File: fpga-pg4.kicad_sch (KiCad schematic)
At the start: 23 parts, among them U6 XC7A15T-CSG325

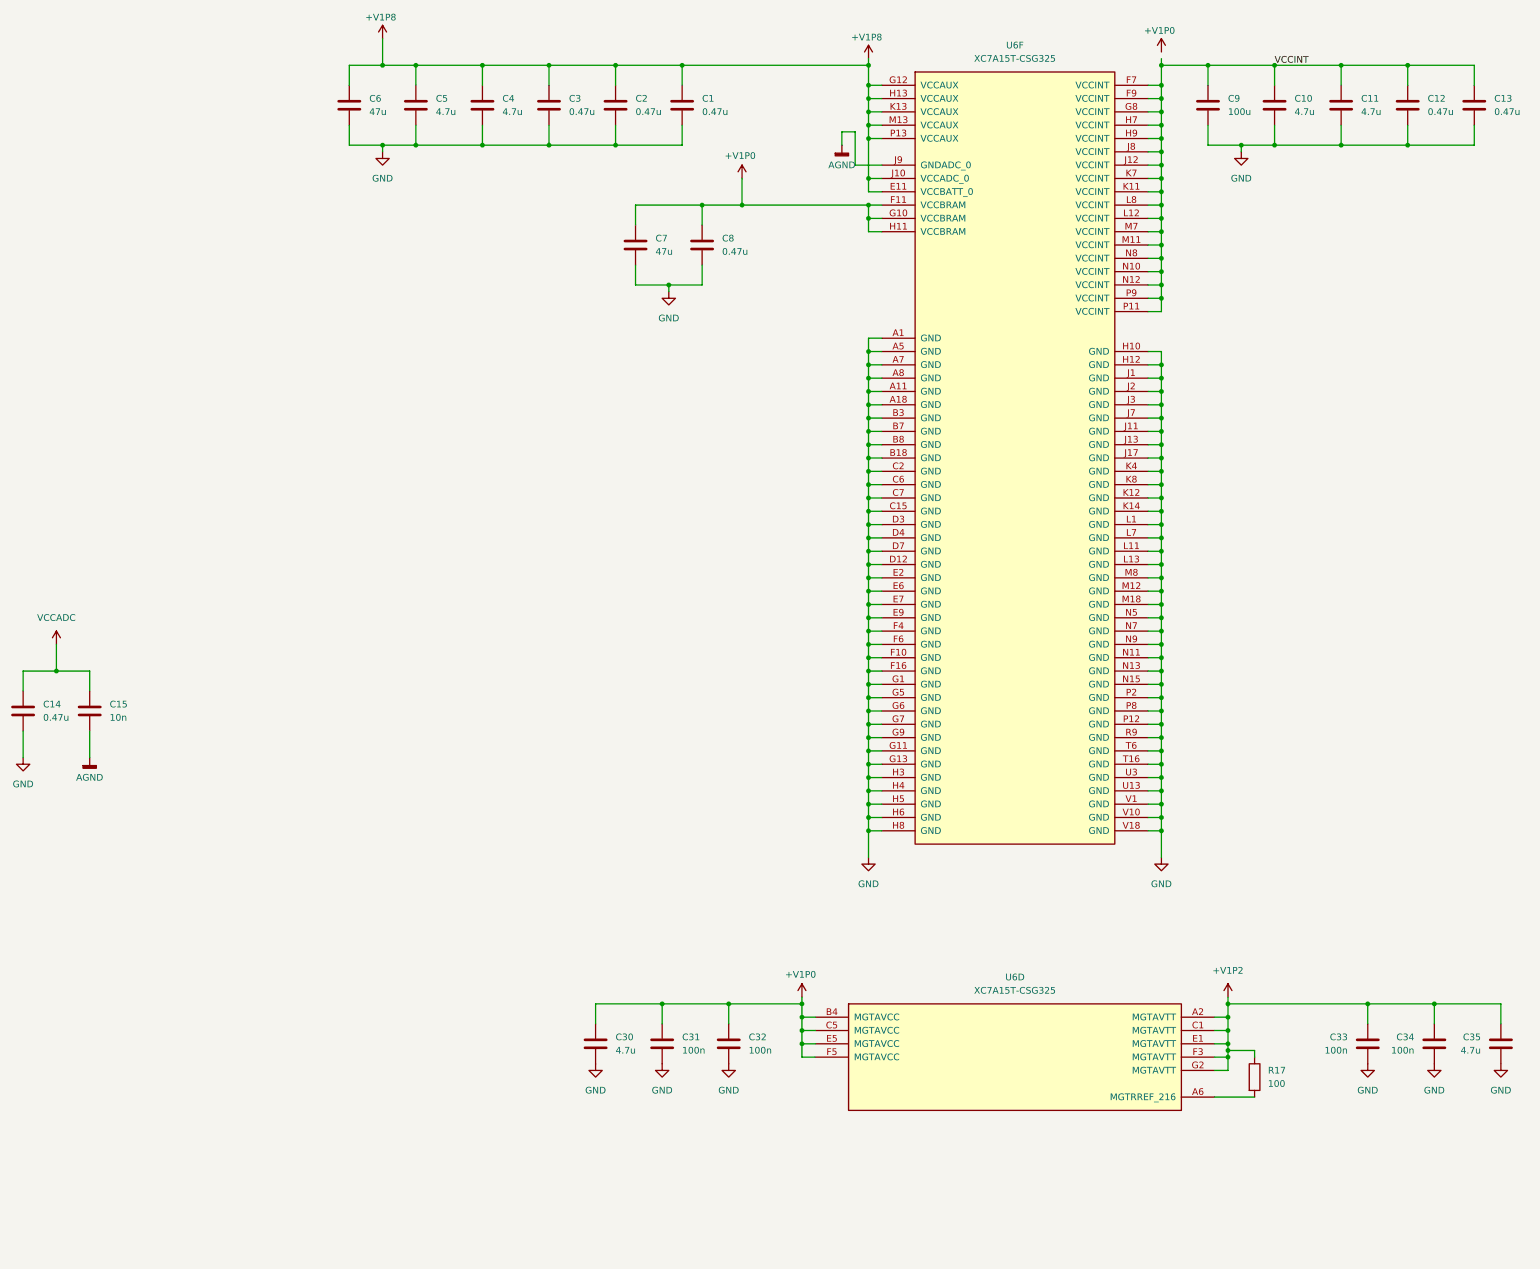
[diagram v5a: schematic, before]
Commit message: started changing package, added correct decoupling
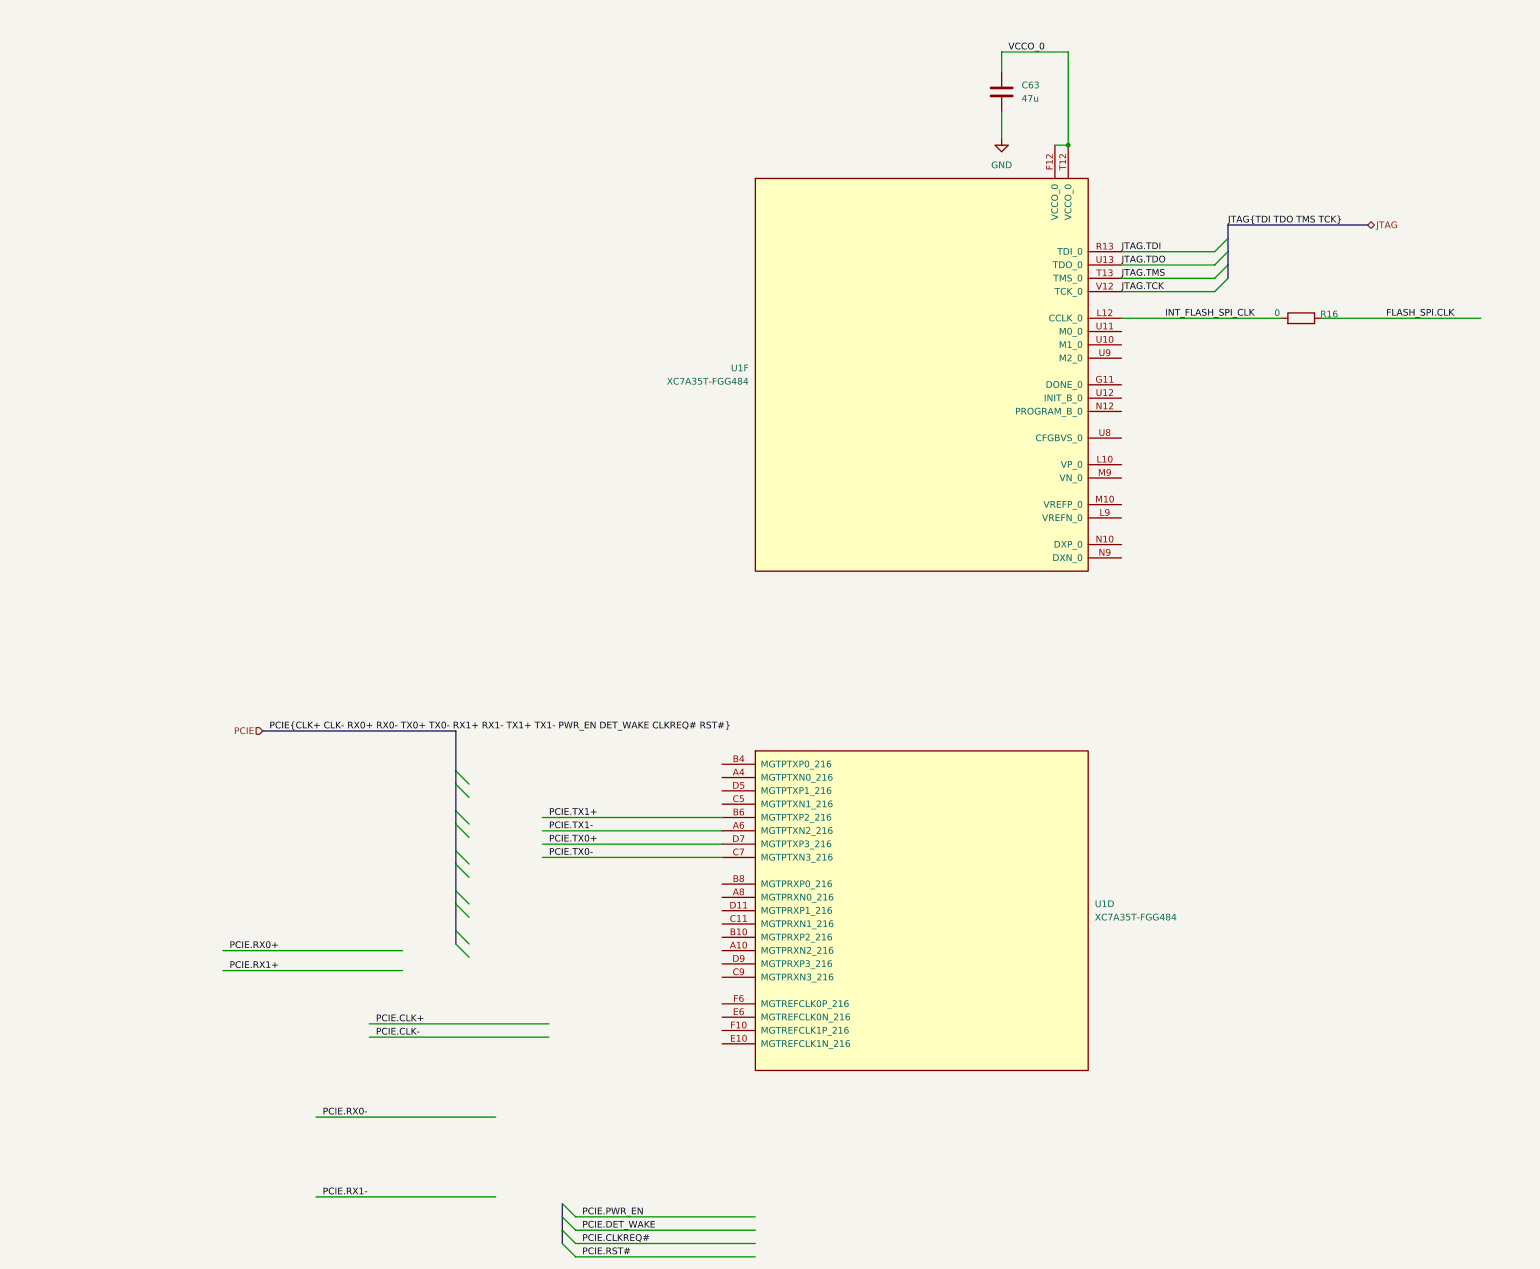
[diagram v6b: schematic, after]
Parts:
- removed C1, C12, C13, C14, C2, C3, C8: 0.47u, Capacitor_SMD:C_0402_1005Metric, symbol Device:C
- removed C10, C11, C30, C35, C4, C5: 4.7u, Capacitor_SMD:C_0402_1005Metric, symbol Device:C
- removed C15: 10n, Capacitor_SMD:C_0402_1005Metric, symbol Device:C
- removed C31, C32, C33, C34: 100n, Capacitor_SMD:C_0402_1005Metric, symbol Device:C
- removed C6, C7: 47u, Capacitor_SMD:C_1210_3225Metric, symbol Device:C
- removed C9: 100u, Capacitor_SMD:C_1210_3225Metric, symbol Device:C
- removed R17: 100, Capacitor_SMD:C_0402_1005Metric, symbol Device:R
- removed U6: XC7A15T-CSG325, Package_BGA:Xilinx_CSG325, symbol FPGA_Xilinx_Artix7:XC7A15T-CSG325
- added C63: 47u, Capacitor_SMD:C_1210_3225Metric, symbol Device:C
- added R16: 0, Resistor_SMD:R_0402_1005Metric_Pad0.72x0.64mm_HandSolder, symbol Device:R
- added U1: XC7A35T-FGG484, Package_BGA:Xilinx_FGG484, symbol FPGA_Xilinx_Artix7:XC7A35T-FGG484
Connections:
- net GND: now also C63.2
- new net FLASH_SPI.CLK: R16.1
- new net INT_FLASH_SPI_CLK: R16.2, U1.L12 (CCLK_0)
- new net JTAG.TCK: U1.V12 (TCK_0)
- new net JTAG.TDI: U1.R13 (TDI_0)
- new net JTAG.TDO: U1.U13 (TDO_0)
- new net JTAG.TMS: U1.T13 (TMS_0)
- new net PCIE.TX0+: U1.D7 (MGTPTXP3_216)
- new net PCIE.TX0-: U1.C7 (MGTPTXN3_216)
- new net PCIE.TX1+: U1.B6 (MGTPTXP2_216)
- new net PCIE.TX1-: U1.A6 (MGTPTXN2_216)
- new net VCCO_0: C63.1, U1.F12 (VCCO_0), U1.T12 (VCCO_0)

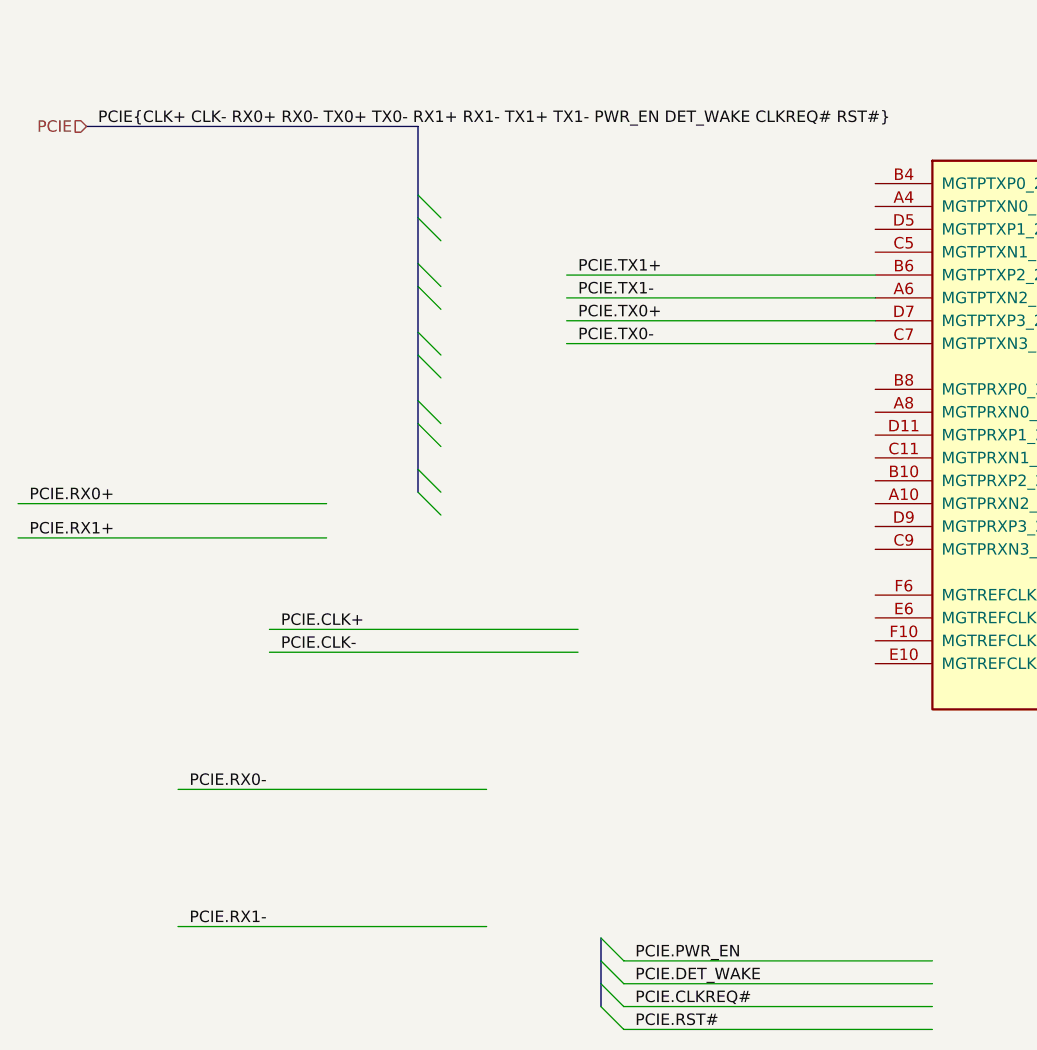
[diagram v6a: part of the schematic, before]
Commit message: filled out back connector, finished ddr pinning according to vivado
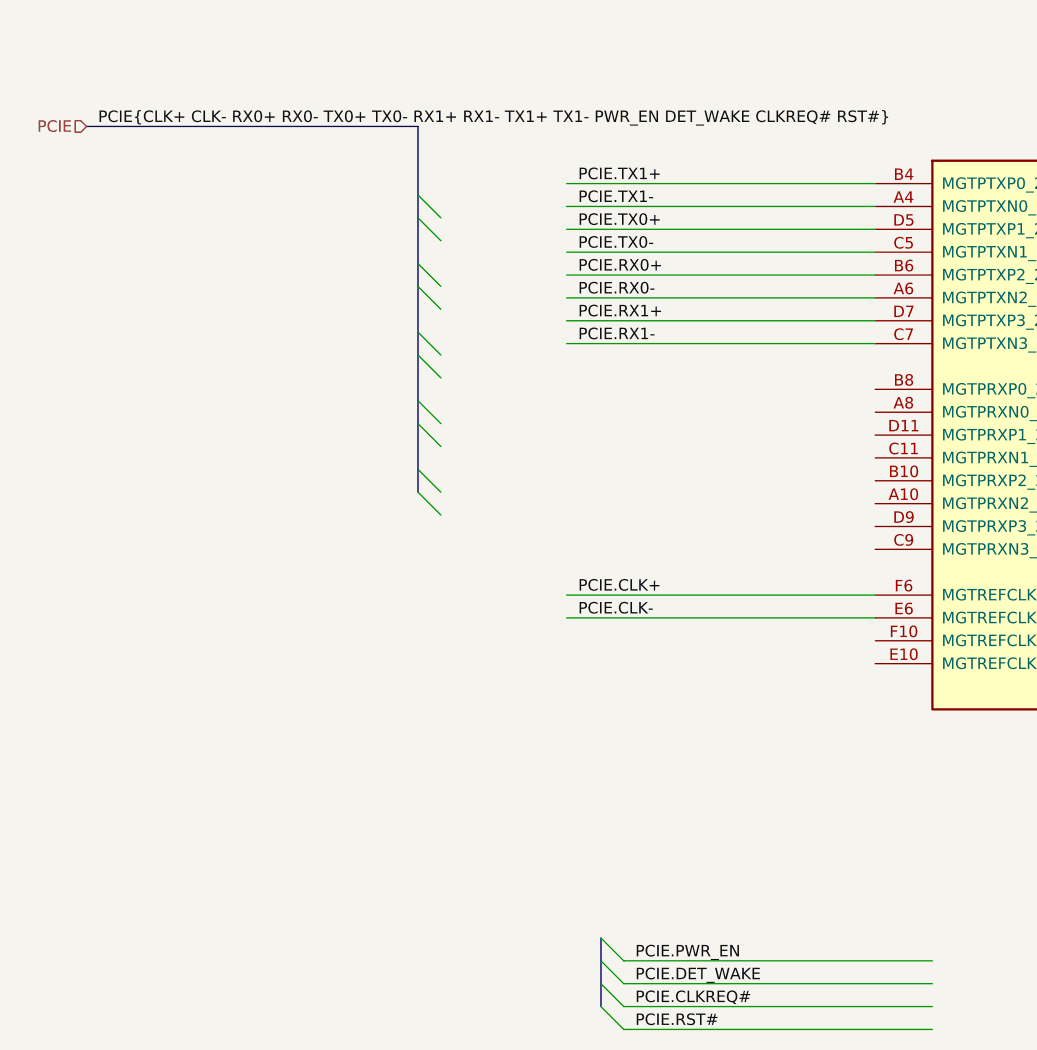
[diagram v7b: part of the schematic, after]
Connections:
- net PCIE.CLK+: now also U1.F6 (MGTREFCLK0P_216)
- net PCIE.CLK-: now also U1.E6 (MGTREFCLK0N_216)
- net PCIE.RX0+: now also U1.B6 (MGTPTXP2_216)
- net PCIE.RX0-: now also U1.A6 (MGTPTXN2_216)
- net PCIE.RX1+: now also U1.D7 (MGTPTXP3_216)
- net PCIE.RX1-: now also U1.C7 (MGTPTXN3_216)
- net PCIE.TX0+: now also U1.D5 (MGTPTXP1_216); no longer U1.D7 (MGTPTXP3_216)
- net PCIE.TX0-: now also U1.C5 (MGTPTXN1_216); no longer U1.C7 (MGTPTXN3_216)
- net PCIE.TX1+: now also U1.B4 (MGTPTXP0_216); no longer U1.B6 (MGTPTXP2_216)
- net PCIE.TX1-: now also U1.A4 (MGTPTXN0_216); no longer U1.A6 (MGTPTXN2_216)
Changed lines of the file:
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@@
+	(wire
+		(pts
+			(xy 137.16 168.91) (xy 171.45 168.91)
+		)
+		(stroke
+			(width 0)
+			(type default)
+		)
+	)
 	(wire
 		(pts
@@
 		)
 	)
+	(wire
+		(pts
+			(xy 137.16 176.53) (xy 171.45 176.53)
+		)
+		(stroke
+			(width 0)
+			(type default)
+		)
+	)
 	(bus
 		(pts
@@
 	(wire
 		(pts
+			(xy 247.65 71.12) (xy 265.43 71.12)
+		)
+		(stroke
+			(width 0)
+			(type default)
+		)
+	)
+	(bus
+		(pts
+			(xy 267.97 71.12) (xy 267.97 68.58)
+		)
+		(stroke
+			(width 0)
+			(type default)
+		)
+	)
+	(bus
+		(pts
+			(xy 140.97 257.81) (xy 140.97 260.35)
+		)
+		(stroke
+			(width 0)
+			(type default)
+		)
+	)
+	(wire
+		(pts
+			(xy 143.51 255.27) (xy 177.8 255.27)
+		)
+		(stroke
+			(width 0)
+			(type default)
+		)
+	)
+	(wire
+		(pts
+			(xy 247.65 78.74) (xy 265.43 78.74)
+		)
+		(stroke
+			(width 0)
+			(type default)
+		)
+	)
+	(wire
+		(pts
+			(xy 247.65 73.66) (xy 265.43 73.66)
+		)
+		(stroke
+			(width 0)
+			(type default)
+		)
+	)
+	(wire
+		(pts
 			(xy 137.16 179.07) (xy 171.45 179.07)
 		)
@@
 		)
 	)
-	(wire
-		(pts
-			(xy 247.65 71.12) (xy 265.43 71.12)
-		)
-		(stroke
-			(width 0)
-			(type default)
-		)
-	)
-	(bus
-		(pts
-			(xy 267.97 71.12) (xy 267.97 68.58)
-		)
-		(stroke
-			(width 0)
-			(type default)
-		)
-	)
-	(wire
-		(pts
-			(xy 76.2 204.47) (xy 110.49 204.47)
-		)
-		(stroke
-			(width 0)
-			(type default)
-		)
-	)
-	(bus
-		(pts
-			(xy 140.97 257.81) (xy 140.97 260.35)
-		)
-		(stroke
-			(width 0)
-			(type default)
-		)
-	)
-	(wire
-		(pts
-			(xy 143.51 255.27) (xy 177.8 255.27)
-		)
-		(stroke
-			(width 0)
-			(type default)
-		)
-	)
-	(wire
-		(pts
-			(xy 247.65 78.74) (xy 265.43 78.74)
-		)
-		(stroke
-			(width 0)
-			(type default)
-		)
-	)
-	(wire
-		(pts
-			(xy 247.65 73.66) (xy 265.43 73.66)
-		)
-		(stroke
-			(width 0)
-			(type default)
-		)
-	)
-	(wire
-		(pts
-			(xy 93.98 251.46) (xy 128.27 251.46)
-		)
-		(stroke
-			(width 0)
-			(type default)
-		)
-	)
 	(bus
 		(pts
@@
 	(wire
 		(pts
-			(xy 93.98 236.22) (xy 128.27 236.22)
+			(xy 137.16 171.45) (xy 171.45 171.45)
 		)
 		(stroke
@@
 		)
 	)
+	(wire
+		(pts
+			(xy 137.16 181.61) (xy 171.45 181.61)
+		)
+		(stroke
+			(width 0)
+			(type default)
+		)
+	)
 	(bus
 		(pts
@@
 		)
 	)
+	(bus
+		(pts
+			(xy 120.65 193.04) (xy 120.65 195.58)
+		)
+		(stroke
+			(width 0)
+			(type default)
+		)
+	)
+	(wire
+		(pts
+			(xy 278.13 83.82) (xy 247.65 83.82)
+		)
+		(stroke
+			(width 0)
+			(type default)
+		)
+	)
 	(wire
 		(pts
@@
 	(wire
 		(pts
-			(xy 137.16 181.61) (xy 171.45 181.61)
-		)
-		(stroke
-			(width 0)
-			(type default)
-		)
-	)
-	(bus
-		(pts
-			(xy 120.65 193.04) (xy 120.65 195.58)
-		)
-		(stroke
-			(width 0)
-			(type default)
-		)
-	)
-	(wire
-		(pts
-			(xy 278.13 83.82) (xy 247.65 83.82)
+			(xy 137.16 184.15) (xy 171.45 184.15)
 		)
 		(stroke
@@
 	(wire
 		(pts
-			(xy 104.14 218.44) (xy 138.43 218.44)
+			(xy 137.16 214.63) (xy 171.45 214.63)
 		)
 		(stroke
@@
 		)
 	)
+	(wire
+		(pts
+			(xy 137.16 173.99) (xy 171.45 173.99)
+		)
+		(stroke
+			(width 0)
+			(type default)
+		)
+	)
 	(bus
 		(pts
@@
 		)
 	)
-	(wire
-		(pts
-			(xy 137.16 184.15) (xy 171.45 184.15)
-		)
-		(stroke
-			(width 0)
-			(type default)
-		)
-	)
 	(bus
 		(pts
@@
 	(wire
 		(pts
-			(xy 104.14 220.98) (xy 138.43 220.98)
+			(xy 137.16 217.17) (xy 171.45 217.17)
 		)
 		(stroke
@@
 		)
 	)
-	(wire
-		(pts
-			(xy 76.2 208.28) (xy 110.49 208.28)
-		)
-		(stroke
-			(width 0)
-			(type default)
-		)
-	)
 	(bus
 		(pts
@@
 			(width 0)
 			(type default)
-		)
-	)
-	(label "PCIE.RX1+"
-		(at 77.47 208.28 0)
-		(effects
-			(font
-				(size 1.27 1.27)
-			)
-			(justify left bottom)
 		)
 	)
@@
 		)
 	)
+	(label "PCIE.CLK-"
+		(at 138.43 217.17 0)
+		(effects
+			(font
+				(size 1.27 1.27)
+			)
+			(justify left bottom)
+		)
+	)
+	(label "PCIE.TX0+"
+		(at 138.43 173.99 0)
+		(effects
+			(font
+				(size 1.27 1.27)
+			)
+			(justify left bottom)
+		)
+	)
 	(label "PCIE.TX0-"
-		(at 138.43 186.69 0)
-		(effects
-			(font
-				(size 1.27 1.27)
-			)
-			(justify left bottom)
-		)
-	)
-	(label "PCIE.CLK-"
-		(at 105.41 220.98 0)
+		(at 138.43 176.53 0)
 		(effects
 			(font
@@
 		)
 	)
-	(label "PCIE.RX1-"
-		(at 95.25 251.46 0)
-		(effects
-			(font
-				(size 1.27 1.27)
-			)
-			(justify left bottom)
-		)
-	)
-	(label "PCIE.RX0-"
-		(at 95.25 236.22 0)
-		(effects
-			(font
-				(size 1.27 1.27)
-			)
-			(justify left bottom)
-		)
-	)
 	(label "PCIE.CLKREQ#"
 		(at 144.78 260.35 0)
@@
 		)
 	)
-	(label "PCIE.TX1-"
-		(at 138.43 181.61 0)
-		(effects
-			(font
-				(size 1.27 1.27)
-			)
-			(justify left bottom)
-		)
-	)
 	(label "PCIE.DET_WAKE"
 		(at 144.78 257.81 0)
@@
 		)
 	)
+	(label "PCIE.RX0-"
+		(at 138.43 181.61 0)
+		(effects
+			(font
+				(size 1.27 1.27)
+			)
+			(justify left bottom)
+		)
+	)
+	(label "PCIE.TX1-"
+		(at 138.43 171.45 0)
+		(effects
+			(font
+				(size 1.27 1.27)
+			)
+			(justify left bottom)
+		)
+	)
 	(label "PCIE.RST#"
 		(at 144.78 262.89 0)
@@
 		)
 	)
+	(label "PCIE.RX1-"
+		(at 138.43 186.69 0)
+		(effects
+			(font
+				(size 1.27 1.27)
+			)
+			(justify left bottom)
+		)
+	)
+	(label "PCIE.TX1+"
+		(at 138.43 168.91 0)
+		(effects
+			(font
+				(size 1.27 1.27)
+			)
+			(justify left bottom)
+		)
+	)
 	(label "PCIE.CLK+"
-		(at 105.41 218.44 0)
+		(at 138.43 214.63 0)
 		(effects
 			(font
@@
 		)
 	)
-	(label "PCIE.TX0+"
-		(at 138.43 184.15 0)
-		(effects
-			(font
-				(size 1.27 1.27)
-			)
-			(justify left bottom)
-		)
-	)
 	(label "FLASH_SPI.CLK"
 		(at 311.15 83.82 180)
@@
 		)
 	)
+	(label "PCIE.RX1+"
+		(at 138.43 184.15 0)
+		(effects
+			(font
+				(size 1.27 1.27)
+			)
+			(justify left bottom)
+		)
+	)
 	(label "PCIE.RX0+"
-		(at 77.47 204.47 0)
-		(effects
-			(font
-				(size 1.27 1.27)
-			)
-			(justify left bottom)
-		)
-	)
-	(label "PCIE.TX1+"
 		(at 138.43 179.07 0)
 		(effects

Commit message: added a lot of stuff
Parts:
- renumbered C63 to C43, R16 to R6
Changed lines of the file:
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@@
 		(dnp no)
 		(fields_autoplaced yes)
-		(property "Reference" "C63"
+		(property "Reference" "C43"
 			(at 228.6 39.3699 0)
 			(effects
@@
 			(project "logix-core"
 				(path "/cf3b7c5f-6ddc-4e3f-9529-0bcf5eec6f23/824409ff-e0aa-4944-ad80-228eadb659f9/0be3540d-0ef7-4890-b983-c7f7caf1a192"
-					(reference "C63")
+					(reference "C43")
 					(unit 1)
 				)
@@
 		(on_board yes)
 		(dnp no)
-		(property "Reference" "R16"
+		(property "Reference" "R6"
 			(at 287.274 83.058 90)
 			(effects
@@
 			(project "logix-core"
 				(path "/cf3b7c5f-6ddc-4e3f-9529-0bcf5eec6f23/824409ff-e0aa-4944-ad80-228eadb659f9/0be3540d-0ef7-4890-b983-c7f7caf1a192"
-					(reference "R16")
+					(reference "R6")
 					(unit 1)
 				)
@@
 		(dnp no)
 		(fields_autoplaced yes)
-		(property "Reference" "#PWR067"
+		(property "Reference" "#PWR07"
 			(at 224.79 55.88 0)
 			(effects
@@
 			(project "logix-core"
 				(path "/cf3b7c5f-6ddc-4e3f-9529-0bcf5eec6f23/824409ff-e0aa-4944-ad80-228eadb659f9/0be3540d-0ef7-4890-b983-c7f7caf1a192"
-					(reference "#PWR067")
+					(reference "#PWR07")
 					(unit 1)
 				)
